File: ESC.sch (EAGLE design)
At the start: 45 parts, among them U1 AMS1117-3.3

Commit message: blank
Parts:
- added U$1: TERMINAL3, TRANS_IRF3205SPBF:TERMINAL3
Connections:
- net N$10: now also U$1.A
- net N$13: now also U$1.B
- net N$23: now also U$1.C
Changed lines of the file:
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@@
 <?xml version="1.0" encoding="utf-8"?>
 <!DOCTYPE eagle SYSTEM "eagle.dtd">
-<eagle version="9.1.2">
+<eagle version="8.3.2">
 <drawing>
 <settings>
@@
 <part name="SUPPLY11" library="SparkFun-PowerSymbols" deviceset="5V" device=""/>
 <part name="OLED1" library="TRANS_IRF3205SPBF" deviceset="I2C_OLED_4PIN_HEADER" device=""/>
+<part name="U$1" library="TRANS_IRF3205SPBF" deviceset="TERMINAL3" device=""/>
 </parts>
 <sheets>
@@
 <instance part="SUPPLY11" gate="G$1" x="-35.56" y="10.16"/>
 <instance part="OLED1" gate="G$1" x="-73.66" y="-25.4"/>
+<instance part="U$1" gate="G$1" x="200.66" y="7.62"/>
 </instances>
 <busses>
@@
 <wire x1="137.16" y1="-48.26" x2="149.86" y2="-48.26" width="0.1524" layer="91"/>
 <wire x1="149.86" y1="-48.26" x2="149.86" y2="-45.72" width="0.1524" layer="91"/>
-<wire x1="149.86" y1="-45.72" x2="157.48" y2="-45.72" width="0.1524" layer="91"/>
 <wire x1="149.86" y1="-48.26" x2="149.86" y2="-50.8" width="0.1524" layer="91"/>
 <junction x="149.86" y="-48.26"/>
 <pinref part="R0805_N2" gate="G$1" pin="1"/>
 <wire x1="152.4" y1="-50.8" x2="149.86" y2="-50.8" width="0.1524" layer="91"/>
+<wire x1="149.86" y1="-45.72" x2="182.88" y2="-45.72" width="0.1524" layer="91"/>
+<wire x1="182.88" y1="-45.72" x2="182.88" y2="12.7" width="0.1524" layer="91"/>
+<pinref part="U$1" gate="G$1" pin="A"/>
+<wire x1="182.88" y1="12.7" x2="195.58" y2="12.7" width="0.1524" layer="91"/>
 </segment>
 </net>
@@
 <pinref part="TC2" gate="G$1" pin="VS"/>
 <wire x1="114.3" y1="15.24" x2="111.76" y2="15.24" width="0.1524" layer="91"/>
-<wire x1="149.86" y1="7.62" x2="157.48" y2="7.62" width="0.1524" layer="91"/>
 <wire x1="149.86" y1="7.62" x2="149.86" y2="5.08" width="0.1524" layer="91"/>
 <pinref part="R0805_N6" gate="G$1" pin="1"/>
@@
 <wire x1="137.16" y1="5.08" x2="149.86" y2="5.08" width="0.1524" layer="91"/>
 <junction x="149.86" y="5.08"/>
+<wire x1="149.86" y1="7.62" x2="195.58" y2="7.62" width="0.1524" layer="91"/>
+<pinref part="U$1" gate="G$1" pin="B"/>
 </segment>
 </net>
@@
 <pinref part="TC3" gate="G$1" pin="VS"/>
 <wire x1="114.3" y1="68.58" x2="111.76" y2="68.58" width="0.1524" layer="91"/>
-<wire x1="149.86" y1="60.96" x2="157.48" y2="60.96" width="0.1524" layer="91"/>
 <wire x1="149.86" y1="60.96" x2="149.86" y2="58.42" width="0.1524" layer="91"/>
 <pinref part="R0805_N10" gate="G$1" pin="1"/>
@@
 <wire x1="137.16" y1="58.42" x2="149.86" y2="58.42" width="0.1524" layer="91"/>
 <junction x="149.86" y="58.42"/>
-</segment>
-</net>
+<wire x1="149.86" y1="60.96" x2="185.42" y2="60.96" width="0.1524" layer="91"/>
+<wire x1="185.42" y1="60.96" x2="185.42" y2="2.54" width="0.1524" layer="91"/>
+<pinref part="U$1" gate="G$1" pin="C"/>
+<wire x1="185.42" y1="2.54" x2="195.58" y2="2.54" width="0.1524" layer="91"/>
+</segment>
+</net>

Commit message: lastest edits
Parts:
- removed ARDUINO_NANO_SPOT1: ARDUINO_NANO_CONNECTOR, TRANS_IRF3205SPBF:ARDUINO_NANO_CONNECTOR
- removed C0603_N10: 0.1uF, SparkFun-Capacitors:0.1UF-0603-25V-5%
- removed C0603_N20: 22pF, SparkFun-Capacitors:22PF-0603-50V-5%
- removed C0805_N5, C0805_N6: 22uF, SparkFun-Capacitors:22UF-0805-6.3V-20%
- removed D6: 1N4001, 1N4001:1N4001
- added NANO_SPOT1: (no value), TRANS_IRF3205SPBF:ARDUINO_NANO_CONNECTOR
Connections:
- net N$10 renamed A_OUT
- net N$13 renamed B_OUT
- net N$23 renamed C_OUT
- removed net N$16: ARDUINO_NANO_SPOT1.12
- removed net N$20: ARDUINO_NANO_SPOT1.24, TC2.HIN
- removed net N$25: ARDUINO_NANO_SPOT1.28, TC3.HIN
- removed net N$26: ARDUINO_NANO_SPOT1.29, TC3.LIN
- removed net N$30: ARDUINO_NANO_SPOT1.6, R0805_N10.2, R0805_N9.1
- removed net N$31: ARDUINO_NANO_SPOT1.7, POT.S
- removed net N$5: ARDUINO_NANO_SPOT1.21, TC1.HIN
- removed net N$7: ARDUINO_NANO_SPOT1.4, R0805_N1.1, R0805_N2.2
- removed net N$8: ARDUINO_NANO_SPOT1.23, TC1.LIN
- removed net N$9: ARDUINO_NANO_SPOT1.27, TC2.LIN
- new net 5V_OUT: NANO_SPOT1.+5V, OLED1.VCC
- new net AREF: NANO_SPOT1.A0, R0805_N1.1, R0805_N2.2
- new net A_HI: TC1.HIN
- new net A_LO: TC1.LIN
- new net BREF: NANO_SPOT1.A1, R0805_N5.1, R0805_N6.2
- new net B_HI: TC2.HIN
- new net B_LO: TC2.LIN
- new net CREF: NANO_SPOT1.A2, R0805_N10.2, R0805_N9.1
- new net C_HI: TC3.HIN
- new net C_LO: TC3.LIN
- new net N$32: POT.S
- new net N$36: NANO_SPOT1.VIN
- new net N$41: NANO_SPOT1.D5
- new net N$42: NANO_SPOT1.D4
- new net N$43: NANO_SPOT1.D8
- new net N$44: NANO_SPOT1.D7
- new net N$45: NANO_SPOT1.D2
- new net N$46: NANO_SPOT1.D3
- new net N$47: NANO_SPOT1.D6
- new net N$48: NANO_SPOT1.D9
- new net SCL: NANO_SPOT1.SCL, OLED1.SCL
- new net SDA: NANO_SPOT1.SDA, OLED1.SDA
- net GND: now also NANO_SPOT1.GND, NANO_SPOT1.GRND, OLED1.GND; no longer ARDUINO_NANO_SPOT1.14
- net N$2: now also NANO_SPOT1.SS; no longer ARDUINO_NANO_SPOT1.5, R0805_N5.1, R0805_N6.2
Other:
- moved on the sheet: C0603_N1, C0603_N2, C0603_N3, C0603_N4, C0603_N5, C0603_N6, C0805_N1, C0805_N2, C0805_N3, C0805_N4, C1, CTH_N1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

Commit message: daily updates 10022018
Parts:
- added FAN1: 2P_POWER, TRANS_IRF3205SPBF:2P_POWER
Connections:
- net 5V_OUT: now also FAN1.VIN
- net GND: now also FAN1.GND
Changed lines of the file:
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@@
 <part name="NANO_SPOT1" library="TRANS_IRF3205SPBF" deviceset="ARDUINO_NANO_CONNECTOR" device=""/>
 <part name="GND22" library="TRANS_IRF3205SPBF" deviceset="GND" device=""/>
+<part name="FAN1" library="TRANS_IRF3205SPBF" deviceset="2P_POWER" device=""/>
+<part name="GND24" library="TRANS_IRF3205SPBF" deviceset="GND" device=""/>
 </parts>
 <sheets>
@@
 <instance part="NANO_SPOT1" gate="G$1" x="-43.18" y="-20.32"/>
 <instance part="GND22" gate="1" x="-53.34" y="2.54"/>
+<instance part="FAN1" gate="G$1" x="7.62" y="33.02"/>
+<instance part="GND24" gate="1" x="-2.54" y="25.4"/>
 </instances>
 <busses>
@@
 <junction x="-53.34" y="7.62"/>
 <pinref part="GND22" gate="1" pin="GND"/>
+</segment>
+<segment>
+<pinref part="FAN1" gate="G$1" pin="GND"/>
+<wire x1="0" y1="30.48" x2="-2.54" y2="30.48" width="0.1524" layer="91"/>
+<wire x1="-2.54" y1="30.48" x2="-2.54" y2="27.94" width="0.1524" layer="91"/>
+<pinref part="GND24" gate="1" pin="GND"/>
 </segment>
 </net>
@@
 <label x="-88.9" y="30.48" size="1.778" layer="95" rot="R180" xref="yes"/>
 </segment>
-</net>
+<segment>
+<pinref part="FAN1" gate="G$1" pin="VIN"/>
+<wire x1="0" y1="35.56" x2="-2.54" y2="35.56" width="0.1524" layer="91"/>
+<label x="-2.54" y="35.56" size="1.778" layer="95" rot="R180" xref="yes"/>
+</segment>
+</net>

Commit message: daily changes for 10042018
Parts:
- removed C0603_N1, C0603_N2, C0603_N3, C0603_N4, C0603_N5, C0603_N6: 0.1uF, SparkFun-Capacitors:0.1UF-0603-25V-5%
- removed C0805_N1, C0805_N2, C0805_N3, C0805_N4: 22uF, SparkFun-Capacitors:22UF-0805-6.3V-20%
- removed CTH_N1: 100uF, SparkFun-Capacitors:100UF-POLAR-RADIAL-2.5MM-25V-20%
- added C10, C12, C13, C4, C6, C7, C9: .1uF, TRANS_IRF3205SPBF:CAPACITORCERAMIC
- added C11, C3, C5, C8: 22uF, TRANS_IRF3205SPBF:CAPACITORSMALL
- added C2: 100uF, TRANS_IRF3205SPBF:CAPACITORSMALL
- added U$2, U$5, U$6, U$7: (no value), TRANS_IRF3205SPBF:LED
- added U$3: BOAT_SWITCH, TRANS_IRF3205SPBF:BOAT_SWITCH
- added U$4: BARREL_JACK, TRANS_IRF3205SPBF:BARREL_JACK
- added U$8: (no value), TRANS_IRF3205SPBF:RESISTOR
- C1: device resistor:CPOL-USE7.5-16 -> TRANS_IRF3205SPBF:CAPACITORLARGE
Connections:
- removed net 5V: CTH_N1.+, POT.E, U1.PIN4, U1.VOUT
- removed net N$2: NANO_SPOT1.SS
- removed net N$32: POT.S
- removed net N$36: NANO_SPOT1.VIN
- removed net N$41: NANO_SPOT1.D5
- removed net N$42: NANO_SPOT1.D4
- removed net N$43: NANO_SPOT1.D8
- removed net N$44: NANO_SPOT1.D7
- removed net N$45: NANO_SPOT1.D2
- removed net N$46: NANO_SPOT1.D3
- removed net N$47: NANO_SPOT1.D6
- removed net N$48: NANO_SPOT1.D9
- removed net VDD: C0805_N4.1, U1.VIN
- new net N$10: U$7.A, U$8.1
- new net N$5: R0805_N1.2, U$2.A
- new net N$7: R0805_N5.2, U$5.A
- new net N$9: R0805_N9.2, U$6.A
- new net POT: NANO_SPOT1.D8, POT.S
- new net POWER: C1.1, C11.1, C12.1, C3.1, C4.1, C5.1, C6.1, C8.1, C9.1, D1.ANODE, D2.ANODE, D3.ANODE, IRF1.D, IRF3.D, IRF5.D, TC1.VCC, TC2.VCC, TC3.VCC, U$3.-, U$8.2, U1.VIN
- new net VIN: C2.1, NANO_SPOT1.VIN, U1.PIN4, U1.VOUT
- net 12V: now also U$3.+, U$4.1; no longer C0603_N1.2, C0603_N3.2, C0603_N5.2, C0805_N1.1, C0805_N2.1, C0805_N3.1, C1.+, D1.ANODE, D2.ANODE, D3.ANODE, IRF1.D, IRF3.D, IRF5.D, TC1.VCC, TC2.VCC, TC3.VCC
- net 5V_OUT: now also POT.E
- net A_HI: now also NANO_SPOT1.D2
- net A_LO: now also NANO_SPOT1.D3
- net A_OUT: now also C7.2; no longer C0603_N2.2
- net B_HI: now also NANO_SPOT1.D4
- net B_LO: now also NANO_SPOT1.D5
- net B_OUT: now also C10.2; no longer C0603_N4.2
- net C_HI: now also NANO_SPOT1.D6
- net C_LO: now also NANO_SPOT1.D7
- net C_OUT: now also C13.2; no longer C0603_N6.2
- net GND: now also C1.2, C11.2, C12.2, C2.2, C3.2, C4.2, C5.2, C6.2, C8.2, C9.2, U$2.C, U$4.3, U$5.C, U$6.C, U$7.C; no longer C0603_N1.1, C0603_N3.1, C0603_N5.1, C0805_N1.2, C0805_N2.2, C0805_N3.2, C0805_N4.2, C1.-, CTH_N1.-, R0805_N1.2, R0805_N5.2, R0805_N9.2
- net N$11: now also C7.1; no longer C0603_N2.1
- net N$19: now also C10.1; no longer C0603_N4.1
- net N$29: now also C13.1; no longer C0603_N6.1
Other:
- moved on the sheet: NANO_SPOT1

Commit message: daily updates 10052018
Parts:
- removed R0805_N1, R0805_N5, R0805_N9: 1Kohm, TRANS_IRF3205SPBF:R1KOHM_0805
- removed R0805_N10, R0805_N2, R0805_N6: 2Kohm, TRANS_IRF3205SPBF:R2KOHM_0805
- removed R0805_N11, R0805_N3, R0805_N7: 100ohm, TRANS_IRF3205SPBF:R100OHM_0805
- removed R0805_N12, R0805_N4, R0805_N8: (no value), TRANS_IRF3205SPBF:R100OHM_0805
- added R10, R11, R12, R13, R2, R3, R4, R5, R6, R7, R8, R9: (no value), TRANS_IRF3205SPBF:RESISTOR
- renumbered U$1 to TERMINAL_OUT, U$8 to R1
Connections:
- net AREF: now also R4.2, R5.1; no longer R0805_N1.1, R0805_N2.2
- net A_OUT: now also R4.1; no longer R0805_N2.1
- net BREF: now also R8.2, R9.1; no longer R0805_N5.1, R0805_N6.2
- net B_OUT: now also R8.1; no longer R0805_N6.1
- net CREF: now also R12.2, R13.1; no longer R0805_N10.2, R0805_N9.1
- net C_OUT: now also R12.1; no longer R0805_N10.1
- net N$1: now also R3.2; no longer R0805_N4.2
- net N$12: now also R6.2; no longer R0805_N7.2
- net N$14: now also R7.2; no longer R0805_N8.2
- net N$17: now also R6.1; no longer R0805_N7.1
- net N$18: now also R7.1; no longer R0805_N8.1
- net N$22: now also R10.2; no longer R0805_N11.2
- net N$24: now also R11.2; no longer R0805_N12.2
- net N$27: now also R10.1; no longer R0805_N11.1
- net N$28: now also R11.1; no longer R0805_N12.1
- net N$3: now also R2.1; no longer R0805_N3.1
- net N$4: now also R2.2; no longer R0805_N3.2
- net N$5: now also R5.2; no longer R0805_N1.2
- net N$6: now also R3.1; no longer R0805_N4.1
- net N$7: now also R9.2; no longer R0805_N5.2
- net N$9: now also R13.2; no longer R0805_N9.2

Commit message: late changes 10052018
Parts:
- removed IRF2, IRF4, IRF6: (no value), TRANS_IRF3205SPBF:IRF3205
- removed U1: AMS1117-3.3, AMS1117-3.3:AMS1117-3.3
- added AZ1117CH5.0: AZ1117CH, TRANS_IRF3205SPBF:AZ1117CH
- added IRF3205PBF-ND_2, IRF3205PBF-ND_4, IRF3205PBF-ND_6: (no value), TRANS_IRF3205SPBF:IRF3205
- R10, R11, R2, R3, R6, R7: value (none) -> 100Ohm
- R12, R4, R8: value (none) -> 2kOhm
- R13, R5, R9: value (none) -> 1kOhm
- renumbered IRF1 to IRF3205PBF-ND_1, IRF3 to IRF3205PBF-ND_3, IRF5 to IRF3205PBF-ND_5, TC1 to IR2301PBF-ND_1, TC2 to IR2301PBF-ND_2, TC3 to IR2301PBF-ND_3
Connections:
- net A_OUT: now also IRF3205PBF-ND_2.D; no longer IRF2.D
- net B_OUT: now also IRF3205PBF-ND_4.D; no longer IRF4.D
- net C_OUT: now also IRF3205PBF-ND_6.D; no longer IRF6.D
- net GND: now also AZ1117CH5.0.ADJ/GND, IRF3205PBF-ND_2.S, IRF3205PBF-ND_4.S, IRF3205PBF-ND_6.S; no longer IRF2.S, IRF4.S, IRF6.S, U1.ADJ/GND
- net N$1: now also IRF3205PBF-ND_2.G; no longer IRF2.G
- net N$14: now also IRF3205PBF-ND_4.G; no longer IRF4.G
- net N$24: now also IRF3205PBF-ND_6.G; no longer IRF6.G
- net POWER: now also AZ1117CH5.0.IN; no longer U1.VIN
- net VIN: now also AZ1117CH5.0.OUT; no longer U1.PIN4, U1.VOUT

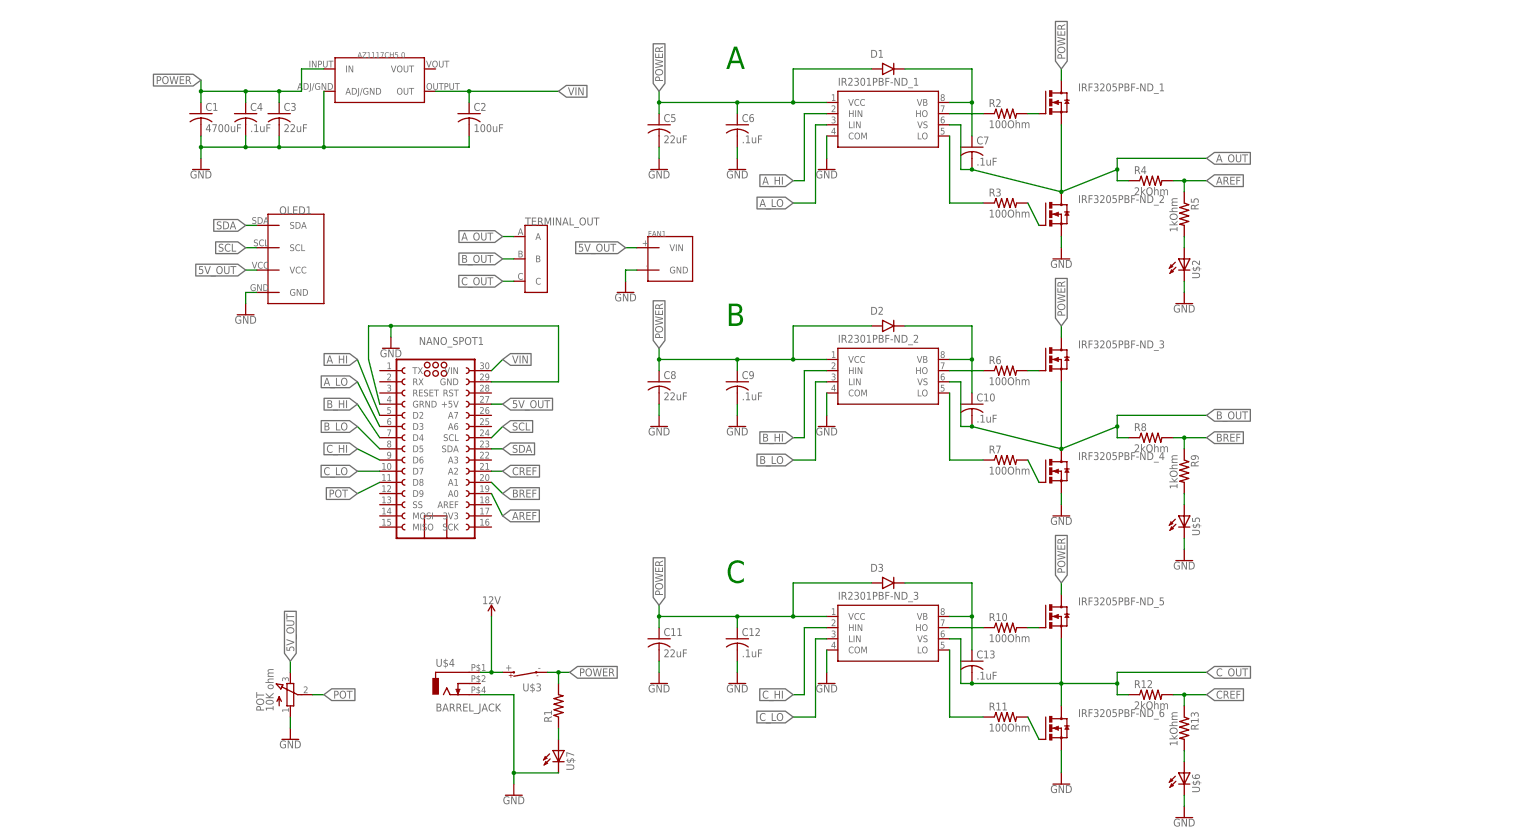
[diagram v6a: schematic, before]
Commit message: finalized schematic
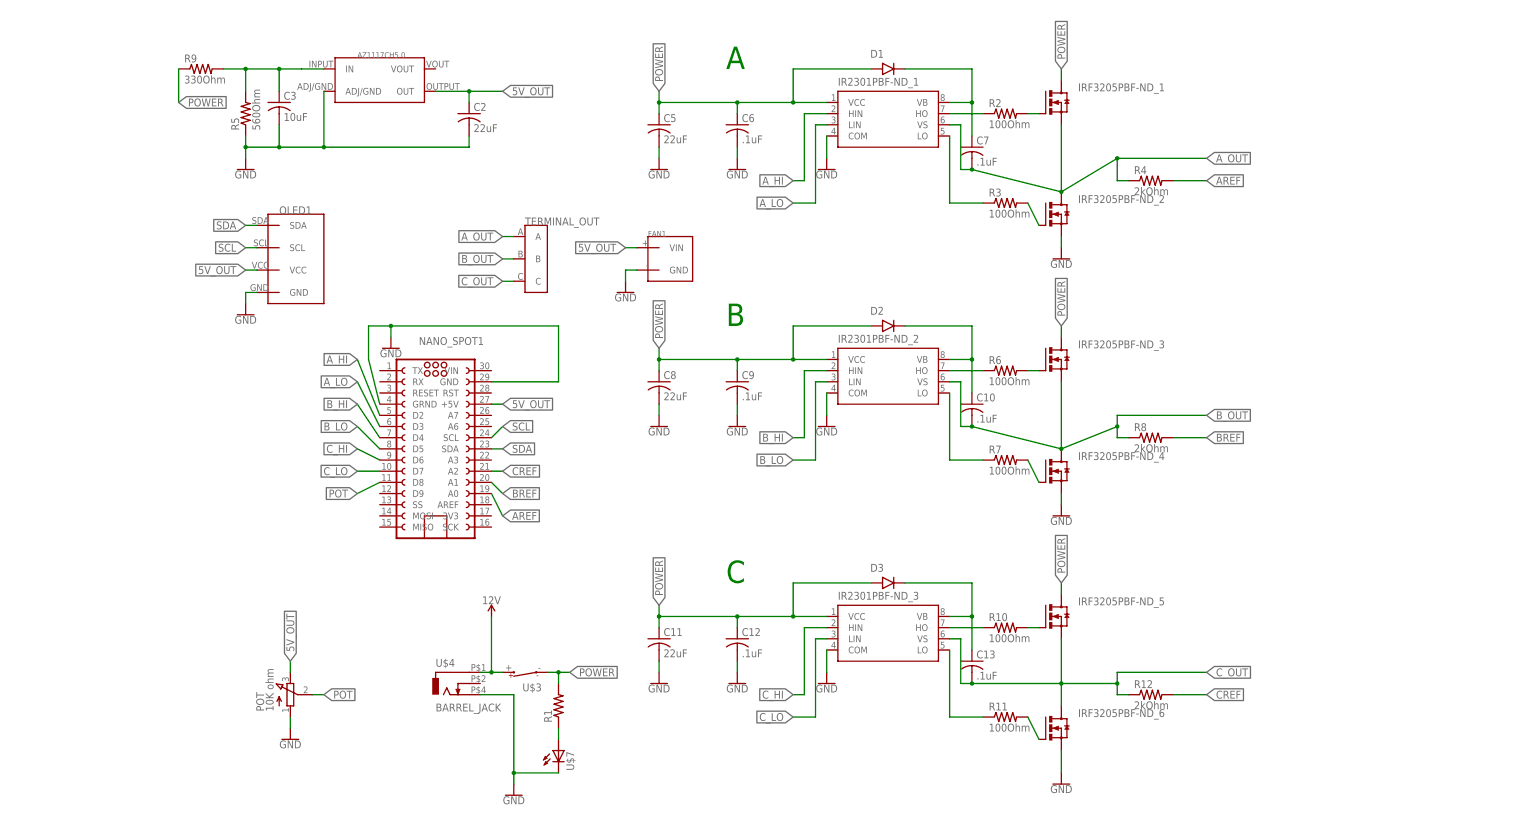
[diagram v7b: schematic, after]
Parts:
- removed C1: 4700uF, TRANS_IRF3205SPBF:CAPACITORLARGE
- removed C4: .1uF, TRANS_IRF3205SPBF:CAPACITORCERAMIC
- removed R13: 1kOhm, TRANS_IRF3205SPBF:RESISTOR
- removed U$2, U$5, U$6: (no value), TRANS_IRF3205SPBF:LED
- C2: value 100uF -> 22uF
- C3: value 22uF -> 10uF
- R5: value 1kOhm -> 560Ohm
- R9: value 1kOhm -> 330Ohm
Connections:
- removed net N$5: R5.2, U$2.A
- removed net N$7: R9.2, U$5.A
- removed net N$9: R13.2, U$6.A
- removed net VIN: AZ1117CH5.0.OUT, C2.1, NANO_SPOT1.VIN
- net 5V_OUT: now also AZ1117CH5.0.OUT, C2.1
- net AREF: no longer R5.1
- net BREF: no longer R9.1
- net CREF: no longer R13.1
- net GND: now also R5.1; no longer C1.2, C4.2, U$2.C, U$5.C, U$6.C
- net POWER: now also R5.2, R9.1, R9.2; no longer C1.1, C4.1
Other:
- moved on the sheet: C3, R5, R9
